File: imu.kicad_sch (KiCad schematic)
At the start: 17 parts, among them U2 BNO086, Y1 32.768khz

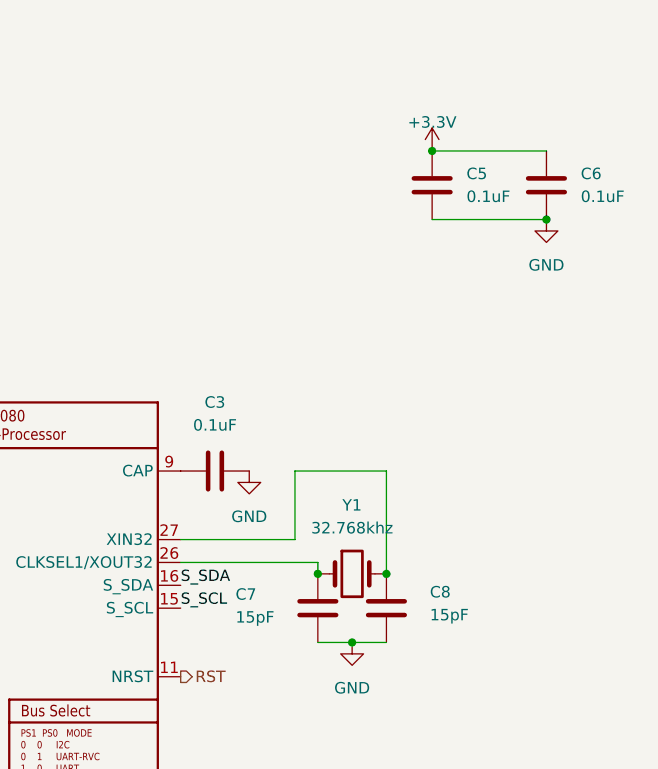
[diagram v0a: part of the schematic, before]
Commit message: remove efuse
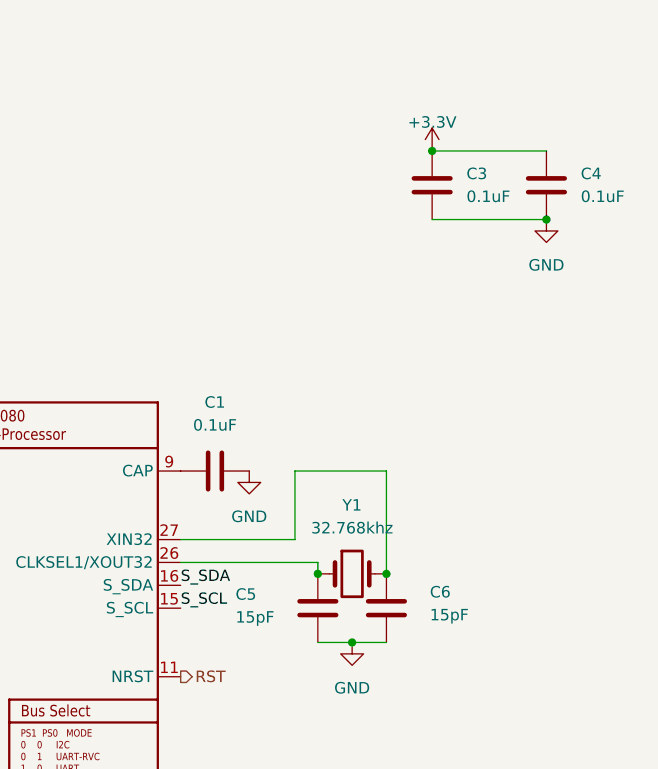
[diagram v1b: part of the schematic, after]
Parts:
- renumbered C3 to C1, C5 to C3, C6 to C4, C7 to C5, C8 to C6
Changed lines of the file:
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@@
 		(on_board yes)
 		(dnp no)
-		(property "Reference" "C8"
+		(property "Reference" "C6"
 			(at 188.976 108.712 0)
 			(effects
@@
 			(project "mainboard4"
 				(path "/dd07ab80-a59c-44f4-ac7d-849e21e1384e/96c222f9-4b91-4480-a910-25e2ecb9014a"
-					(reference "C8")
+					(reference "C6")
 					(unit 1)
 				)
@@
 		(dnp no)
 		(fields_autoplaced yes)
-		(property "Reference" "C6"
+		(property "Reference" "C4"
 			(at 205.74 62.2299 0)
 			(effects
@@
 			(project "mainboard4"
 				(path "/dd07ab80-a59c-44f4-ac7d-849e21e1384e/96c222f9-4b91-4480-a910-25e2ecb9014a"
-					(reference "C6")
+					(reference "C4")
 					(unit 1)
 				)
@@
 		(on_board yes)
 		(dnp no)
-		(property "Reference" "C7"
+		(property "Reference" "C5"
 			(at 167.386 108.966 0)
 			(effects
@@
 			(project "mainboard4"
 				(path "/dd07ab80-a59c-44f4-ac7d-849e21e1384e/96c222f9-4b91-4480-a910-25e2ecb9014a"
-					(reference "C7")
+					(reference "C5")
 					(unit 1)
 				)
@@
 		(dnp no)
 		(fields_autoplaced yes)
-		(property "Reference" "C5"
+		(property "Reference" "C3"
 			(at 193.04 62.2299 0)
 			(effects
@@
 			(project "mainboard4"
 				(path "/dd07ab80-a59c-44f4-ac7d-849e21e1384e/96c222f9-4b91-4480-a910-25e2ecb9014a"
-					(reference "C5")
+					(reference "C3")
 					(unit 1)
 				)
@@
 		(dnp no)
 		(fields_autoplaced yes)
-		(property "Reference" "C3"
+		(property "Reference" "C1"
 			(at 165.1 87.63 90)
 			(effects
@@
 			(project "mainboard4"
 				(path "/dd07ab80-a59c-44f4-ac7d-849e21e1384e/96c222f9-4b91-4480-a910-25e2ecb9014a"
-					(reference "C3")
-					(unit 1)
-				)
+					(reference "C1")
+					(unit 1)
+				)

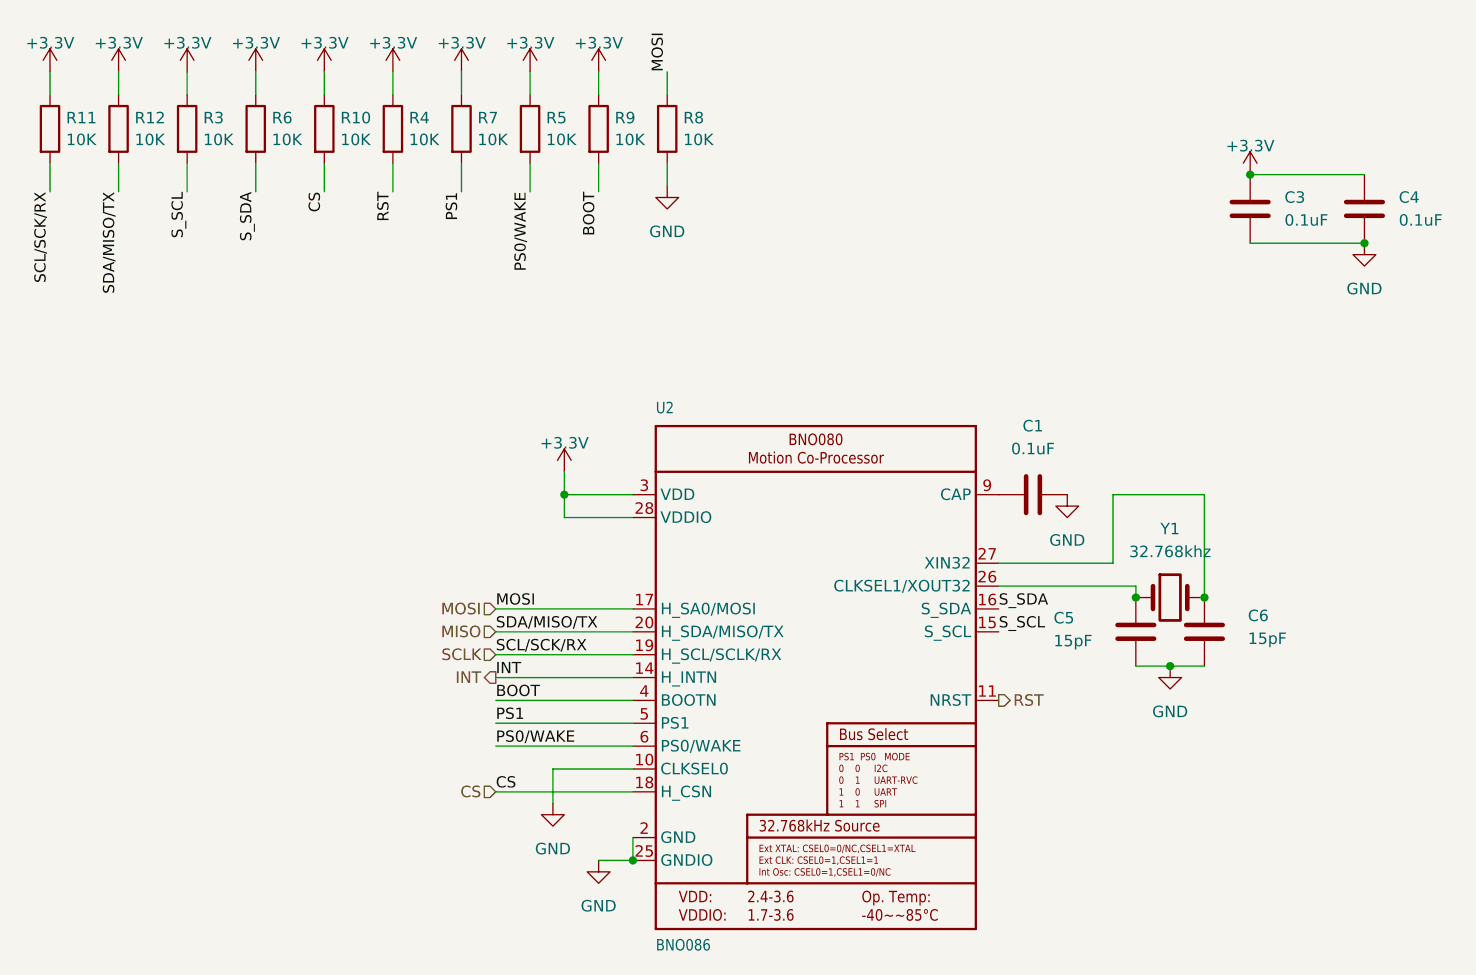
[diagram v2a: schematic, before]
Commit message: add sata capacitor
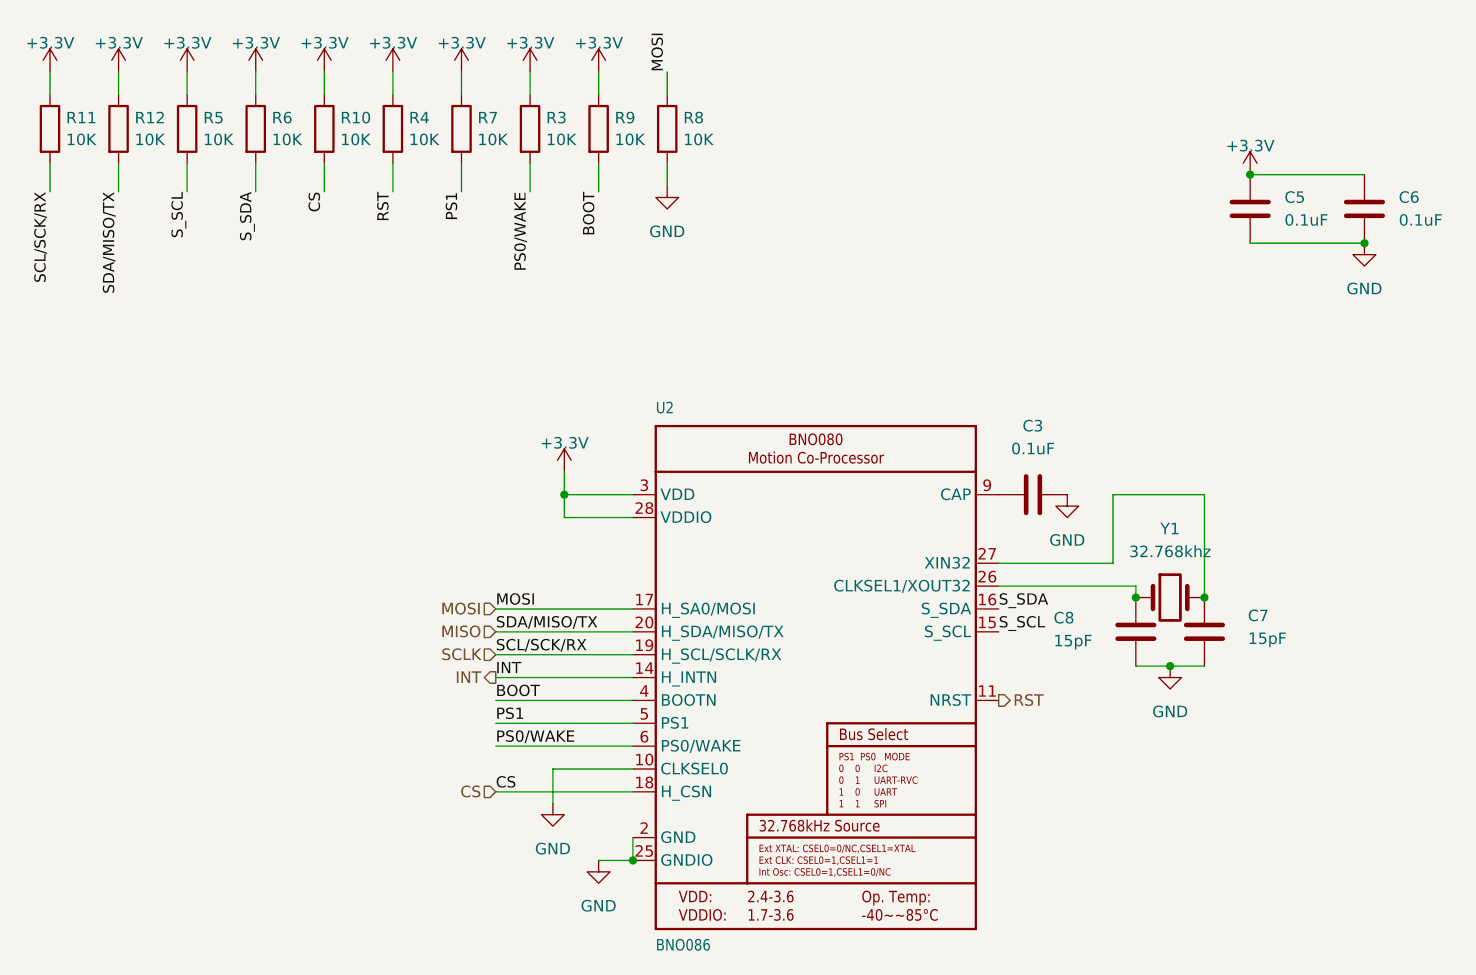
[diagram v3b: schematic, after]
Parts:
- renumbered C1 to C3, C3 to C5, C4 to C6, C6 to C7, C5 to C8, R5 to R3, R3 to R5
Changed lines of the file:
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@@
 	(label "CS"
 		(at 105.41 128.27 0)
+		(fields_autoplaced yes)
 		(effects
 			(font
@@
 	(label "PS1"
 		(at 101.6 61.595 270)
+		(fields_autoplaced yes)
 		(effects
 			(font
@@
 	(label "S_SCL"
 		(at 161.29 110.49 0)
+		(fields_autoplaced yes)
 		(effects
 			(font
@@
 	(label "SDA/MISO/TX"
 		(at 105.41 110.49 0)
+		(fields_autoplaced yes)
 		(effects
 			(font
@@
 	(label "BOOT"
 		(at 116.84 61.595 270)
+		(fields_autoplaced yes)
 		(effects
 			(font
@@
 	(label "PS1"
 		(at 105.41 120.65 0)
+		(fields_autoplaced yes)
 		(effects
 			(font
@@
 	(label "CS"
 		(at 86.36 61.595 270)
+		(fields_autoplaced yes)
 		(effects
 			(font
@@
 	(label "MOSI"
 		(at 124.46 48.26 90)
+		(fields_autoplaced yes)
 		(effects
 			(font
@@
 	(label "S_SDA"
 		(at 78.74 61.595 270)
+		(fields_autoplaced yes)
 		(effects
 			(font
@@
 	(label "RST"
 		(at 93.98 61.595 270)
+		(fields_autoplaced yes)
 		(effects
 			(font
@@
 	(label "PS0{slash}WAKE"
 		(at 105.41 123.19 0)
+		(fields_autoplaced yes)
 		(effects
 			(font
@@
 	(label "SDA/MISO/TX"
 		(at 63.5 61.595 270)
+		(fields_autoplaced yes)
 		(effects
 			(font
@@
 	(label "S_SDA"
 		(at 161.29 107.95 0)
+		(fields_autoplaced yes)
 		(effects
 			(font
@@
 	(label "PS0{slash}WAKE"
 		(at 109.22 61.595 270)
+		(fields_autoplaced yes)
 		(effects
 			(font
@@
 	(label "SCL/SCK/RX"
 		(at 105.41 113.03 0)
+		(fields_autoplaced yes)
 		(effects
 			(font
@@
 	(label "SCL/SCK/RX"
 		(at 55.88 61.595 270)
+		(fields_autoplaced yes)
 		(effects
 			(font
@@
 	(label "MOSI"
 		(at 105.41 107.95 0)
+		(fields_autoplaced yes)
 		(effects
 			(font
@@
 	(label "BOOT"
 		(at 105.41 118.11 0)
+		(fields_autoplaced yes)
 		(effects
 			(font
@@
 	(label "INT"
 		(at 105.41 115.57 0)
+		(fields_autoplaced yes)
 		(effects
 			(font
@@
 	(label "S_SCL"
 		(at 71.12 61.595 270)
+		(fields_autoplaced yes)
 		(effects
 			(font
@@
 		(shape input)
 		(at 105.41 128.27 180)
+		(fields_autoplaced yes)
 		(effects
 			(font
@@
 		(shape input)
 		(at 105.41 107.95 180)
+		(fields_autoplaced yes)
 		(effects
 			(font
@@
 		(shape input)
 		(at 105.41 113.03 180)
+		(fields_autoplaced yes)
 		(effects
 			(font
@@
 		(shape input)
 		(at 105.41 110.49 180)
+		(fields_autoplaced yes)
 		(effects
 			(font
@@
 		(shape output)
 		(at 105.41 115.57 180)
+		(fields_autoplaced yes)
 		(effects
 			(font
@@
 		(shape output)
 		(at 161.29 118.11 0)
+		(fields_autoplaced yes)
 		(effects
 			(font
@@
 		(on_board yes)
 		(dnp no)
-		(property "Reference" "C6"
+		(property "Reference" "C7"
 			(at 188.976 108.712 0)
 			(effects
@@
 			(project "mainboard4"
 				(path "/dd07ab80-a59c-44f4-ac7d-849e21e1384e/96c222f9-4b91-4480-a910-25e2ecb9014a"
-					(reference "C6")
+					(reference "C7")
 					(unit 1)
 				)
@@
 		(dnp no)
 		(fields_autoplaced yes)
-		(property "Reference" "C4"
+		(property "Reference" "C6"
 			(at 205.74 62.2299 0)
 			(effects
@@
 			(project "mainboard4"
 				(path "/dd07ab80-a59c-44f4-ac7d-849e21e1384e/96c222f9-4b91-4480-a910-25e2ecb9014a"
-					(reference "C4")
+					(reference "C6")
 					(unit 1)
 				)
@@
 		(dnp no)
 		(fields_autoplaced yes)
-		(property "Reference" "R3"
+		(property "Reference" "R5"
 			(at 72.898 53.3979 0)
 			(effects
@@
 			(project "mainboard4"
 				(path "/dd07ab80-a59c-44f4-ac7d-849e21e1384e/96c222f9-4b91-4480-a910-25e2ecb9014a"
-					(reference "R3")
+					(reference "R5")
 					(unit 1)
 				)
@@
 		(dnp no)
 		(fields_autoplaced yes)
-		(property "Reference" "R5"
+		(property "Reference" "R3"
 			(at 110.998 53.3979 0)
 			(effects
@@
 			(project "mainboard4"
 				(path "/dd07ab80-a59c-44f4-ac7d-849e21e1384e/96c222f9-4b91-4480-a910-25e2ecb9014a"
-					(reference "R5")
+					(reference "R3")
 					(unit 1)
 				)
@@
 		(on_board yes)
 		(dnp no)
-		(property "Reference" "C5"
+		(property "Reference" "C8"
 			(at 167.386 108.966 0)
 			(effects
@@
 			(project "mainboard4"
 				(path "/dd07ab80-a59c-44f4-ac7d-849e21e1384e/96c222f9-4b91-4480-a910-25e2ecb9014a"
-					(reference "C5")
+					(reference "C8")
 					(unit 1)
 				)
@@
 		(dnp no)
 		(fields_autoplaced yes)
-		(property "Reference" "C3"
+		(property "Reference" "C5"
 			(at 193.04 62.2299 0)
 			(effects
@@
 			(project "mainboard4"
 				(path "/dd07ab80-a59c-44f4-ac7d-849e21e1384e/96c222f9-4b91-4480-a910-25e2ecb9014a"
-					(reference "C3")
+					(reference "C5")
 					(unit 1)
 				)
@@
 		(dnp no)
 		(fields_autoplaced yes)
-		(property "Reference" "C1"
+		(property "Reference" "C3"
 			(at 165.1 87.63 90)
 			(effects
@@
 			(project "mainboard4"
 				(path "/dd07ab80-a59c-44f4-ac7d-849e21e1384e/96c222f9-4b91-4480-a910-25e2ecb9014a"
-					(reference "C1")
-					(unit 1)
-				)
+					(reference "C3")
+					(unit 1)
+				)

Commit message: add logo
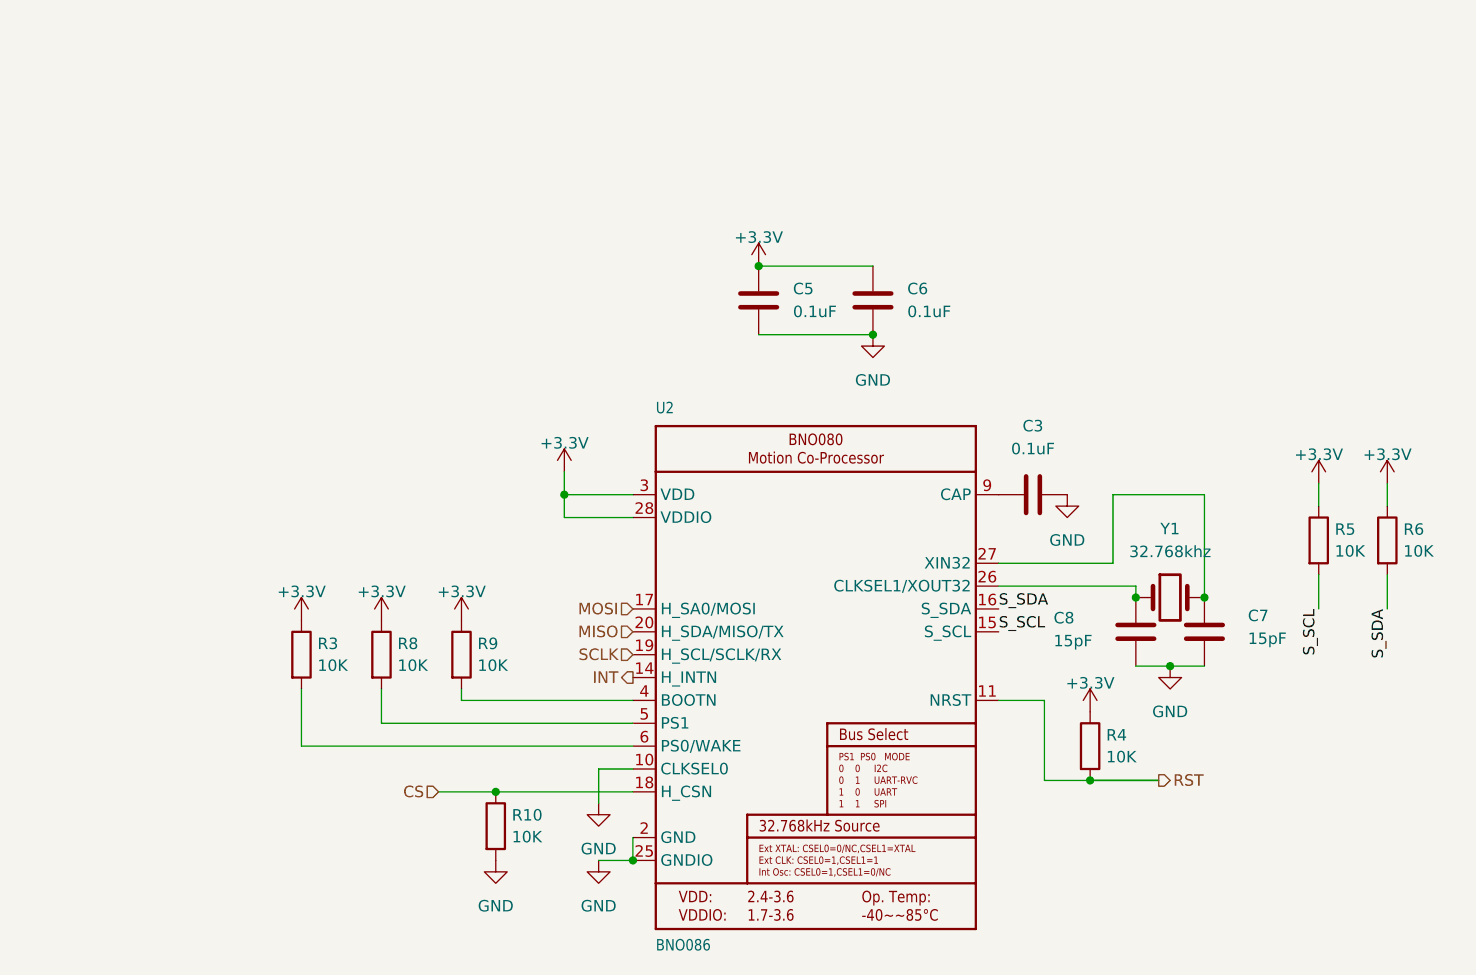
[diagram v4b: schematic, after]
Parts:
- removed R11, R12, R7: 10K, Resistor_SMD:R_0603_1608Metric_Pad0.98x0.95mm_HandSolder, symbol Device:R
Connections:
- net +3.3V: now also R8.1; no longer R10.1
- net CS: now also R10.1; no longer R10.2
- net GND: now also R10.2; no longer R8.2
- net MOSI: no longer R8.1
- net BOOT: no longer names the net of R9.2, U2.4 (BOOTN)
- net PS0/WAKE: no longer names the net of R3.2, U2.6 (PS0/WAKE)
- net PS1: no longer names the net of U2.5 (PS1)
- net PS1: now also R8.2
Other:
- moved on the sheet: C5, C6, R10, R3, R4, R5, R6, R9

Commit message: add logp
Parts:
- renumbered R8 to R7, R9 to R8, R10 to R9
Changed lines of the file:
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@@
 	(label "S_SCL"
 		(at 161.29 110.49 0)
-		(fields_autoplaced yes)
 		(effects
 			(font
@@
 	(label "S_SDA"
 		(at 204.47 107.95 270)
-		(fields_autoplaced yes)
 		(effects
 			(font
@@
 	(label "S_SDA"
 		(at 161.29 107.95 0)
-		(fields_autoplaced yes)
 		(effects
 			(font
@@
 	(label "S_SCL"
 		(at 196.85 107.95 270)
-		(fields_autoplaced yes)
 		(effects
 			(font
@@
 		(shape input)
 		(at 99.06 128.27 180)
-		(fields_autoplaced yes)
 		(effects
 			(font
@@
 		(shape input)
 		(at 120.65 107.95 180)
-		(fields_autoplaced yes)
 		(effects
 			(font
@@
 		(shape input)
 		(at 120.65 113.03 180)
-		(fields_autoplaced yes)
 		(effects
 			(font
@@
 		(shape input)
 		(at 120.65 110.49 180)
-		(fields_autoplaced yes)
 		(effects
 			(font
@@
 		(shape output)
 		(at 120.65 115.57 180)
-		(fields_autoplaced yes)
 		(effects
 			(font
@@
 		(shape output)
 		(at 179.07 127 0)
-		(fields_autoplaced yes)
 		(effects
 			(font
@@
 		(dnp no)
 		(fields_autoplaced yes)
-		(property "Reference" "R9"
+		(property "Reference" "R8"
 			(at 103.378 111.8179 0)
 			(effects
@@
 			(project "mainboard4"
 				(path "/dd07ab80-a59c-44f4-ac7d-849e21e1384e/96c222f9-4b91-4480-a910-25e2ecb9014a"
-					(reference "R9")
+					(reference "R8")
 					(unit 1)
 				)
@@
 		(dnp no)
 		(fields_autoplaced yes)
-		(property "Reference" "R8"
+		(property "Reference" "R7"
 			(at 94.488 111.8179 0)
 			(effects
@@
 			(project "mainboard4"
 				(path "/dd07ab80-a59c-44f4-ac7d-849e21e1384e/96c222f9-4b91-4480-a910-25e2ecb9014a"
-					(reference "R8")
+					(reference "R7")
 					(unit 1)
 				)
@@
 		(dnp no)
 		(fields_autoplaced yes)
-		(property "Reference" "R10"
+		(property "Reference" "R9"
 			(at 107.188 130.8679 0)
 			(effects
@@
 			(project "mainboard4"
 				(path "/dd07ab80-a59c-44f4-ac7d-849e21e1384e/96c222f9-4b91-4480-a910-25e2ecb9014a"
-					(reference "R10")
-					(unit 1)
-				)
+					(reference "R9")
+					(unit 1)
+				)
